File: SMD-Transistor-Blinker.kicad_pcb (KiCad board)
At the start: 2 copper layers, 19.3 x 14.4 mm, 11 parts, among them J1 Conn_01x02_Pin, Q1 BC846, Q2 BC846

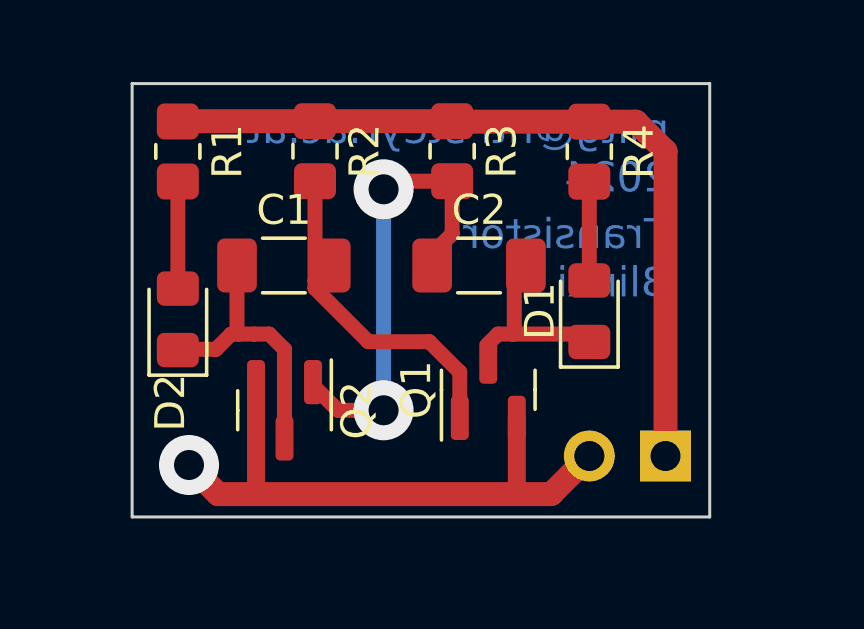
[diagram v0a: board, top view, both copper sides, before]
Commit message: Added QR-Code
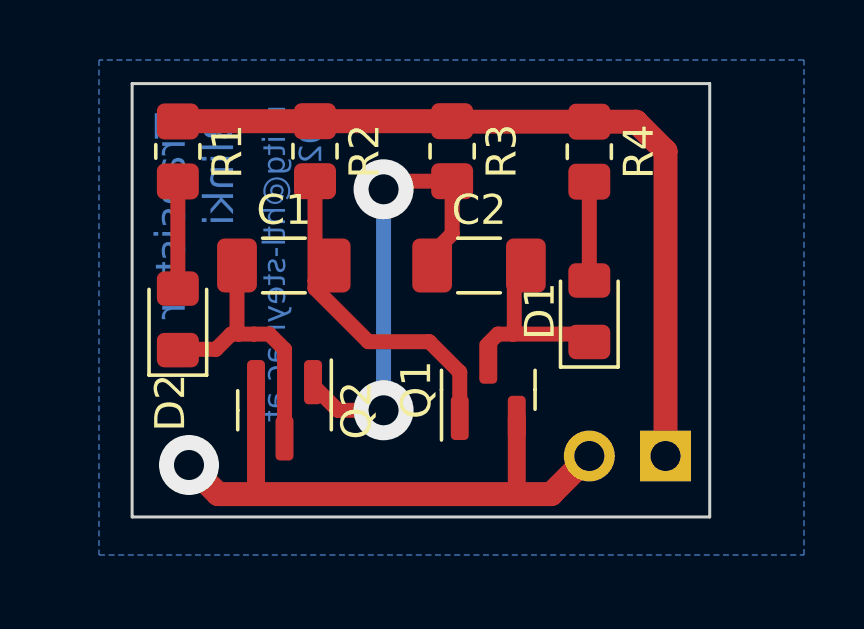
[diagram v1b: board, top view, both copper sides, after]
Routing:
- added copper zone on B.Cu, net (none)

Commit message: added additional ground pin
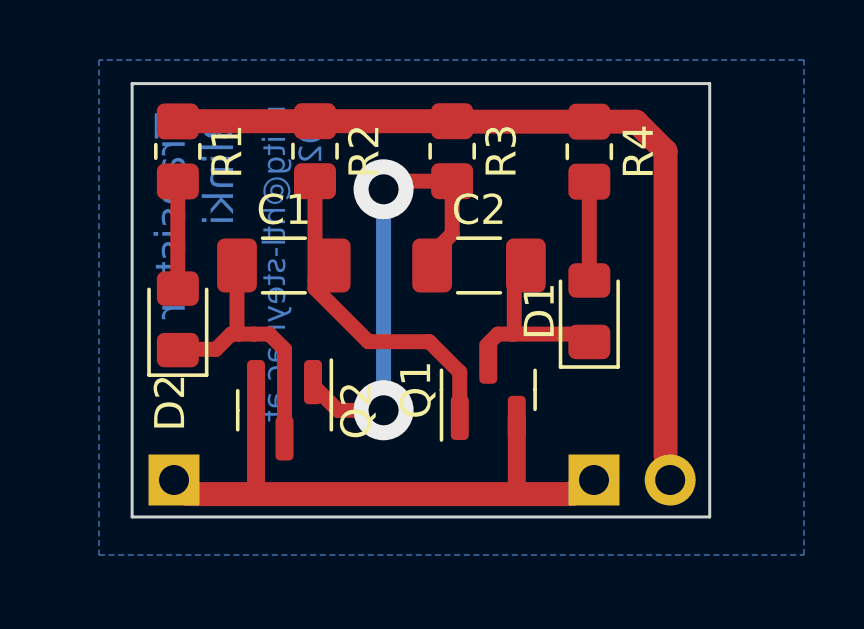
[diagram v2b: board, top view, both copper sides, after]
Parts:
- added J4: PINHD_1x1_Male, Connector_PinHeader_2.54mm:PinHeader_1x01_P2.54mm_Vertical, B.Cu at (135.0, 77.0)
- moved J1 2.51 mm to (149.0, 77.0), turned to -90 degrees
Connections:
- J1 pad 1: +12V -> GND
- J1 pad 2: GND -> +12V
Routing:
- net GND: track 20.5 -> 20.6 mm, vias 1 -> 0

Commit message: Update SMD-Transistor-Blinker.kicad_pcb
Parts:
- moved J4 0.79 mm to (135.2, 76.2)
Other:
- outline, holes or cut-outs redrawn
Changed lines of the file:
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@@
 	(footprint "Connector_PinHeader_2.54mm:PinHeader_1x01_P2.54mm_Vertical"
 		(layer "B.Cu")
-		(at 135 77 180)
+		(at 135.25 76.25 180)
 		(descr "Through hole straight pin header, 1x01, 2.54mm pitch, single row")
 		(tags "Through hole pin header THT 1x01 2.54mm single row")
@@
 		(layer "B.Mask")
 	)
-	(gr_rect
-		(start 133.604 63.786294)
-		(end 152.85767 78.232)
+	(gr_line
+		(start 135.604 63.786294)
+		(end 150.85767 63.786294)
 		(stroke
 			(width 0.1)
 			(type default)
 		)
-		(fill none)
+		(layer "Edge.Cuts")
+	)
+	(gr_line
+		(start 133.604 76.232)
+		(end 133.604 65.786294)
+		(stroke
+			(width 0.1)
+			(type default)
+		)
+		(layer "Edge.Cuts")
+	)
+	(gr_arc
+		(start 135.604 78.232)
+		(mid 134.189786 77.646214)
+		(end 133.604 76.232)
+		(stroke
+			(width 0.1)
+			(type default)
+		)
+		(layer "Edge.Cuts")
+	)
+	(gr_arc
+		(start 133.604 65.786294)
+		(mid 134.189789 64.372084)
+		(end 135.604 63.786294)
+		(stroke
+			(width 0.1)
+			(type default)
+		)
+		(layer "Edge.Cuts")
+	)
+	(gr_line
+		(start 150.85767 78.232)
+		(end 135.604 78.232)
+		(stroke
+			(width 0.1)
+			(type default)
+		)
+		(layer "Edge.Cuts")
+	)
+	(gr_arc
+		(start 152.85767 76.232)
+		(mid 152.271884 77.646214)
+		(end 150.85767 78.232)
+		(stroke
+			(width 0.1)
+			(type default)
+		)
+		(layer "Edge.Cuts")
+	)
+	(gr_arc
+		(start 150.85767 63.786294)
+		(mid 152.271884 64.37208)
+		(end 152.85767 65.786294)
+		(stroke
+			(width 0.1)
+			(type default)
+		)
+		(layer "Edge.Cuts")
+	)
+	(gr_line
+		(start 152.85767 65.786294)
+		(end 152.85767 76.232)
+		(stroke
+			(width 0.1)
+			(type default)
+		)
 		(layer "Edge.Cuts")
 	)
@@
 	)
 	(segment
+		(start 136.47 77.47)
+		(end 135.25 76.25)
+		(width 0.8)
+		(layer "F.Cu")
+		(net 2)
+	)
+	(segment
+		(start 148.265 77.47)
+		(end 136.47 77.47)
+		(width 0.8)
+		(layer "F.Cu")
+		(net 2)
+	)
+	(segment
 		(start 148.844 76.891)
 		(end 148.265 77.47)
 		(width 0.8)
 		(layer "F.Cu")
-		(net 2)
-	)
-	(segment
-		(start 135.47 77.47)
-		(end 135 77)
-		(width 0.8)
-		(layer "F.Cu")
-		(net 2)
-	)
-	(segment
-		(start 148.265 77.47)
-		(end 135.47 77.47)
-		(width 0.8)
-		(layer "F.Cu")

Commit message: optimierung kicad
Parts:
- moved J1 1.52 mm to (148.8, 75.5)
- moved J4 0.35 mm to (135.5, 76.0)
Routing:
- net +12V: track 26.9 -> 26.2 mm
- net Net-(Q2-B): track 15.8 -> 15.2 mm
- added copper zone on B.Cu, net GND
- removed copper zone on B.Cu, net (none)
